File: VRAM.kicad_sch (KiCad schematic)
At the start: 8 parts, among them U801 IDT7134, U802 IDT7134, U803 GAL22V10, U804 74HCT574

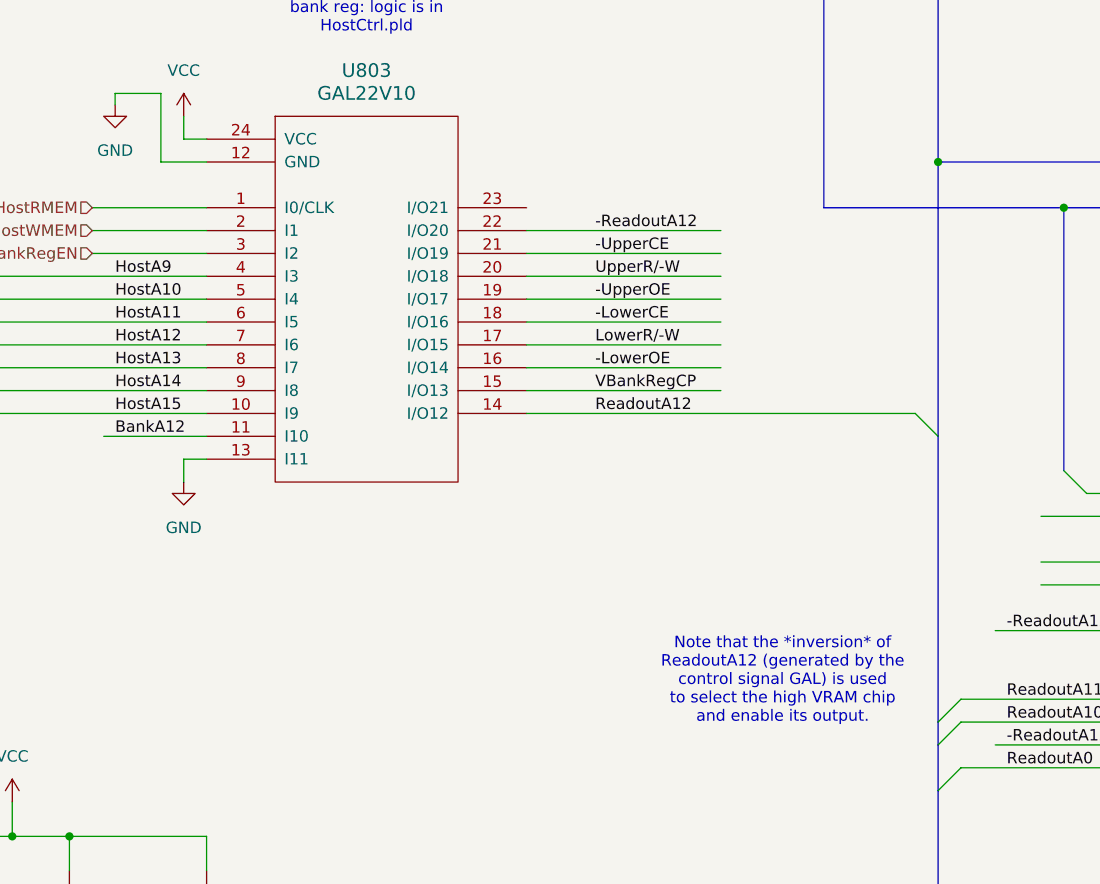
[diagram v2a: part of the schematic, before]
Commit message: avoid using I/O pin as input on control GAL
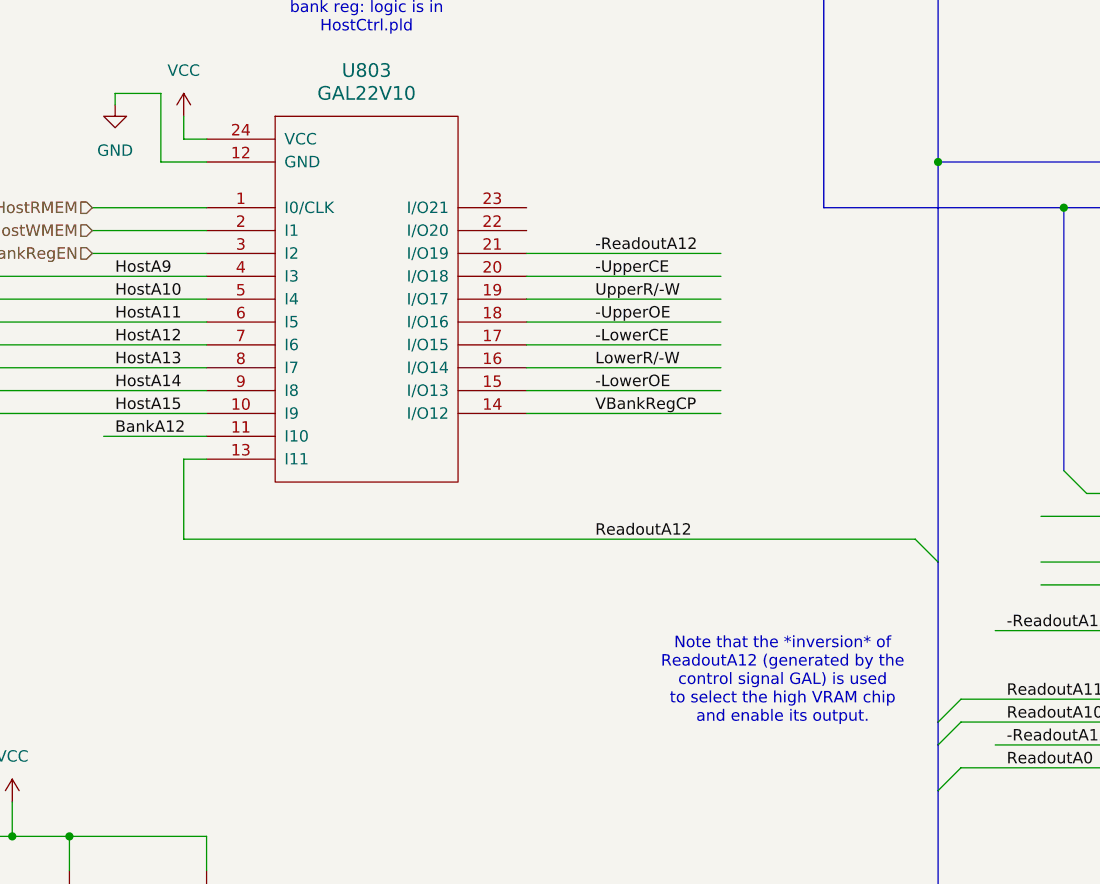
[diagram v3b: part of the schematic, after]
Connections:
- net -LowerCE: now also U803.17 (I/O15); no longer U803.18 (I/O16)
- net -LowerOE: now also U803.15 (I/O13); no longer U803.16 (I/O14)
- net -ReadoutA12: now also U803.21 (I/O19); no longer U803.22 (I/O20)
- net -UpperCE: now also U803.20 (I/O18); no longer U803.21 (I/O19)
- net -UpperOE: now also U803.18 (I/O16); no longer U803.19 (I/O17)
- net GND: no longer U803.13 (I11)
- net LowerR/-W: now also U803.16 (I/O14); no longer U803.17 (I/O15)
- net ReadoutA12: now also U803.13 (I11); no longer U803.14 (I/O12)
- net UpperR/-W: now also U803.19 (I/O17); no longer U803.20 (I/O18)
- net VBankRegCP: now also U803.14 (I/O12); no longer U803.15 (I/O13)
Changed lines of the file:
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@@
 	)
 	(bus_entry
-		(at 161.29 140.97)
-		(size 2.54 2.54)
-		(stroke
-			(width 0)
-			(type default)
-		)
-	)
-	(bus_entry
 		(at 237.49 22.86)
 		(size 2.54 2.54)
@@
 	)
 	(bus_entry
+		(at 161.29 154.94)
+		(size 2.54 2.54)
+		(stroke
+			(width 0)
+			(type default)
+		)
+	)
+	(bus_entry
 		(at 247.65 205.74)
 		(size 2.54 2.54)
@@
 	(wire
 		(pts
-			(xy 25.4 130.81) (xy 38.1 130.81)
+			(xy 80.01 154.94) (xy 161.29 154.94)
 		)
 		(stroke
@@
 	(wire
 		(pts
-			(xy 229.87 205.74) (xy 229.87 193.04)
+			(xy 25.4 130.81) (xy 38.1 130.81)
 		)
 		(stroke
@@
 	(wire
 		(pts
-			(xy 118.11 128.27) (xy 139.7 128.27)
+			(xy 229.87 205.74) (xy 229.87 193.04)
 		)
 		(stroke
@@
 		)
 	)
-	(bus
+	(wire
 		(pts
-			(xy 163.83 213.36) (xy 163.83 215.9)
+			(xy 118.11 130.81) (xy 139.7 130.81)
 		)
 		(stroke
@@
 	(bus
 		(pts
-			(xy 44.45 46.99) (xy 59.69 46.99)
+			(xy 163.83 213.36) (xy 163.83 215.9)
 		)
 		(stroke
@@
 	(bus
 		(pts
-			(xy 40.64 100.33) (xy 40.64 82.55)
+			(xy 44.45 46.99) (xy 59.69 46.99)
 		)
 		(stroke
@@
 		)
 	)
-	(wire
+	(bus
 		(pts
-			(xy 80.01 146.05) (xy 80.01 148.59)
+			(xy 40.64 100.33) (xy 40.64 82.55)
 		)
 		(stroke
@@
 	(wire
 		(pts
-			(xy 118.11 120.65) (xy 139.7 120.65)
+			(xy 118.11 123.19) (xy 139.7 123.19)
 		)
 		(stroke
@@
 	(wire
 		(pts
-			(xy 118.11 133.35) (xy 139.7 133.35)
+			(xy 118.11 135.89) (xy 139.7 135.89)
 		)
 		(stroke
@@
 	(bus
 		(pts
-			(xy 163.83 113.03) (xy 163.83 143.51)
+			(xy 163.83 113.03) (xy 163.83 157.48)
 		)
 		(stroke
@@
 	(wire
 		(pts
-			(xy 118.11 140.97) (xy 161.29 140.97)
+			(xy 80.01 146.05) (xy 80.01 154.94)
 		)
 		(stroke
@@
 	(wire
 		(pts
-			(xy 118.11 138.43) (xy 139.7 138.43)
+			(xy 118.11 140.97) (xy 139.7 140.97)
 		)
 		(stroke
@@
 	(wire
 		(pts
-			(xy 118.11 135.89) (xy 139.7 135.89)
+			(xy 118.11 138.43) (xy 139.7 138.43)
 		)
 		(stroke
@@
 		)
 	)
+	(bus
+		(pts
+			(xy 163.83 157.48) (xy 163.83 175.26)
+		)
+		(stroke
+			(width 0)
+			(type default)
+		)
+	)
 	(wire
 		(pts
@@
 	(wire
 		(pts
-			(xy 118.11 125.73) (xy 139.7 125.73)
+			(xy 118.11 128.27) (xy 139.7 128.27)
 		)
 		(stroke
@@
 	(wire
 		(pts
+			(xy 80.01 146.05) (xy 82.55 146.05)
+		)
+		(stroke
+			(width 0)
+			(type default)
+		)
+	)
+	(wire
+		(pts
 			(xy 294.64 34.29) (xy 307.34 34.29)
 		)
@@
 		)
 	)
-	(bus
-		(pts
-			(xy 163.83 143.51) (xy 163.83 175.26)
-		)
-		(stroke
-			(width 0)
-			(type default)
-		)
-	)
 	(wire
 		(pts
@@
 		)
 	)
-	(wire
-		(pts
-			(xy 82.55 146.05) (xy 80.01 146.05)
-		)
-		(stroke
-			(width 0)
-			(type default)
-		)
-	)
 	(bus
 		(pts
@@
 	(wire
 		(pts
-			(xy 118.11 123.19) (xy 139.7 123.19)
+			(xy 118.11 125.73) (xy 139.7 125.73)
 		)
 		(stroke
@@
 	(wire
 		(pts
-			(xy 118.11 130.81) (xy 139.7 130.81)
+			(xy 118.11 133.35) (xy 139.7 133.35)
 		)
 		(stroke
@@
 	)
 	(label "-ReadoutA12"
-		(at 125.73 120.65 0)
+		(at 125.73 123.19 0)
 		(fields_autoplaced yes)
 		(effects
@@
 	)
 	(label "VBankRegCP"
-		(at 125.73 138.43 0)
+		(at 125.73 140.97 0)
 		(fields_autoplaced yes)
 		(effects
@@
 	)
 	(label "UpperR{slash}-W"
-		(at 125.73 125.73 0)
+		(at 125.73 128.27 0)
 		(fields_autoplaced yes)
 		(effects
@@
 	)
 	(label "-UpperCE"
-		(at 125.73 123.19 0)
+		(at 125.73 125.73 0)
 		(fields_autoplaced yes)
 		(effects
@@
 	)
 	(label "-UpperOE"
-		(at 125.73 128.27 0)
+		(at 125.73 130.81 0)
 		(fields_autoplaced yes)
 		(effects
@@
 	)
 	(label "LowerR{slash}-W"
-		(at 125.73 133.35 0)
+		(at 125.73 135.89 0)
 		(fields_autoplaced yes)
 		(effects
@@
 	)
 	(label "-LowerCE"
-		(at 125.73 130.81 0)
+		(at 125.73 133.35 0)
 		(fields_autoplaced yes)
 		(effects
@@
 	)
 	(label "ReadoutA12"
-		(at 125.73 140.97 0)
+		(at 125.73 154.94 0)
 		(fields_autoplaced yes)
 		(effects
@@
 	)
 	(label "-LowerOE"
-		(at 125.73 135.89 0)
+		(at 125.73 138.43 0)
 		(fields_autoplaced yes)
 		(effects
@@
 					(unit 1)
 				)
-			)
-		)
-	)
-	(symbol
-		(lib_id "power:GND")
-		(at 80.01 148.59 0)
-		(unit 1)
-		(exclude_from_sim no)
-		(in_bom yes)
-		(on_board yes)
-		(dnp no)
-		(fields_autoplaced yes)
-		(property "Reference" "#PWR085"
-			(at 80.01 154.94 0)
-			(effects
-				(font
-					(size 1.27 1.27)
-				)
-				(hide yes)
-			)
-		)
-		(property "Value" "GND"
-			(at 80.01 153.67 0)
-			(effects
-				(font
-					(size 1.27 1.27)
-				)
-			)
-		)
-		(property "Footprint" ""
-			(at 80.01 148.59 0)
-			(effects
-				(font
-					(size 1.27 1.27)
-				)
-				(hide yes)
-			)
-		)
-		(property "Datasheet" ""
-			(at 80.01 148.59 0)
-			(effects
-				(font
-					(size 1.27 1.27)
-				)
-				(hide yes)
-			)
-		)
-		(property "Description" "Power symbol creates a global label with name \"GND\" , ground"
-			(at 80.01 148.59 0)
-			(effects
-				(font
-					(size 1.27 1.27)
-				)
-				(hide yes)
-			)
-		)
-		(pin "1"
-		)
-		(instances
-			(project "HW_VGA"
-				(path "/c4bd4b39-993a-4195-805f-b4de6fa4aea5/5c8f70a9-e360-4ba4-b352-4320618fb690"
-					(reference "#PWR085")
-					(unit 1)
-				)

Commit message: use "VRAMCtrl.pld" as name for VRAM control logic
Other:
- note added: "Decode host control signals, generate control signals for VRAM and bank reg: logic is in VRAMCtrl.pld"
- note removed: "Decode host control signals, generate control signals for VRAM and bank reg: logic is in HostCtrl.pld"
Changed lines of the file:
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@@
 		)
 	)
-	(text "Decode host control\nsignals, generate control\nsignals for VRAM and\nbank reg: logic is in\nHostCtrl.pld"
+	(text "Decode host control\nsignals, generate control\nsignals for VRAM and\nbank reg: logic is in\nVRAMCtrl.pld"
 		(exclude_from_sim no)
 		(at 100.33 93.98 0)

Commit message: use upper bits of bank reg to select font
With 64 KB of font memory, this means that we can
have 8 different fonts.

Also cleaned up a few issues in the pixel generator
module.
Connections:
- net FontA15: now reaches U804.12 (Q7)
- net FontA14: now reaches U804.13 (Q6)
- net FontA13: now reaches U804.14 (Q5)
- net FontA12: now reaches U804.15 (Q4)
- no-connect marks 14 -> 10
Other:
- note added: "VRAM bank register: selects which 2K bank the host is accessing, and also selects which font in the font ROM is in use"
- note removed: "VRAM bank register (selects which 2K bank the host is accessing)"
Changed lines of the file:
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@@
 	)
 	(no_connect
-		(at 99.06 48.26)
-	)
-	(no_connect
-		(at 99.06 50.8)
-	)
-	(no_connect
 		(at 267.97 170.18)
 	)
@@
 	)
 	(no_connect
-		(at 99.06 53.34)
-	)
-	(no_connect
 		(at 196.85 74.93)
 	)
@@
 	)
 	(no_connect
-		(at 99.06 45.72)
-	)
-	(no_connect
 		(at 196.85 59.69)
 	)
@@
 	(wire
 		(pts
+			(xy 99.06 50.8) (xy 113.03 50.8)
+		)
+		(stroke
+			(width 0)
+			(type default)
+		)
+	)
+	(wire
+		(pts
 			(xy 77.47 113.03) (xy 82.55 113.03)
 		)
@@
 		)
 	)
+	(wire
+		(pts
+			(xy 99.06 53.34) (xy 113.03 53.34)
+		)
+		(stroke
+			(width 0)
+			(type default)
+		)
+	)
 	(bus
 		(pts
@@
 	(wire
 		(pts
+			(xy 99.06 45.72) (xy 113.03 45.72)
+		)
+		(stroke
+			(width 0)
+			(type default)
+		)
+	)
+	(wire
+		(pts
 			(xy 242.57 137.16) (xy 242.57 120.65)
 		)
@@
 	(wire
 		(pts
+			(xy 99.06 48.26) (xy 113.03 48.26)
+		)
+		(stroke
+			(width 0)
+			(type default)
+		)
+	)
+	(wire
+		(pts
 			(xy 193.04 39.37) (xy 217.17 39.37)
 		)
@@
 		)
 	)
-	(text "VRAM bank register\n(selects which 2K bank\nthe host is accessing)"
+	(text "VRAM bank register:\nselects which 2K bank\nthe host is accessing,\nand also selects which\nfont in the font ROM\nis in use"
 		(exclude_from_sim no)
-		(at 107.442 25.4 0)
+		(at 100.838 25.146 0)
 		(effects
 			(font
 				(size 1.27 1.27)
 			)
+			(justify left)
 		)
 	)
@@
 		)
 	)
+	(hierarchical_label "FontA13"
+		(shape output)
+		(at 113.03 48.26 0)
+		(fields_autoplaced yes)
+		(effects
+			(font
+				(size 1.27 1.27)
+			)
+			(justify left)
+		)
+	)
 	(hierarchical_label "ReadoutA6"
 		(shape input)
@@
 		)
 	)
+	(hierarchical_label "FontA12"
+		(shape output)
+		(at 113.03 45.72 0)
+		(fields_autoplaced yes)
+		(effects
+			(font
+				(size 1.27 1.27)
+			)
+			(justify left)
+		)
+	)
 	(hierarchical_label "HostA10"
 		(shape input)
@@
 		)
 	)
+	(hierarchical_label "FontA14"
+		(shape output)
+		(at 113.03 50.8 0)
+		(fields_autoplaced yes)
+		(effects
+			(font
+				(size 1.27 1.27)
+			)
+			(justify left)
+		)
+	)
 	(hierarchical_label "HostD3"
 		(shape bidirectional)
@@
 		)
 	)
+	(hierarchical_label "FontA15"
+		(shape output)
+		(at 113.03 53.34 0)
+		(fields_autoplaced yes)
+		(effects
+			(font
+				(size 1.27 1.27)
+			)
+			(justify left)
+		)
+	)
